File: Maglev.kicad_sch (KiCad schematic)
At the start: 33 parts, among them J1 USB_C_Receptacle, J2 691103110002, J3 61300621121, J4 61300821121, U1 WE-TVS-82400102, U2 ESP32-C3

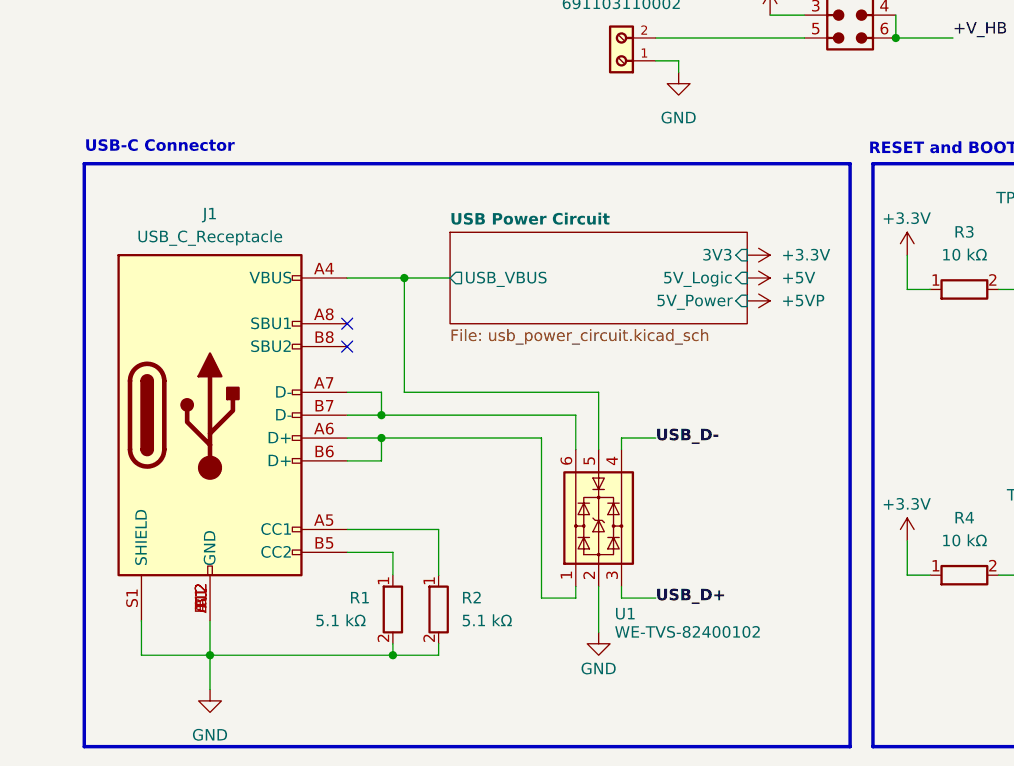
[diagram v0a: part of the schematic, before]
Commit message: cleared some rule checker errors
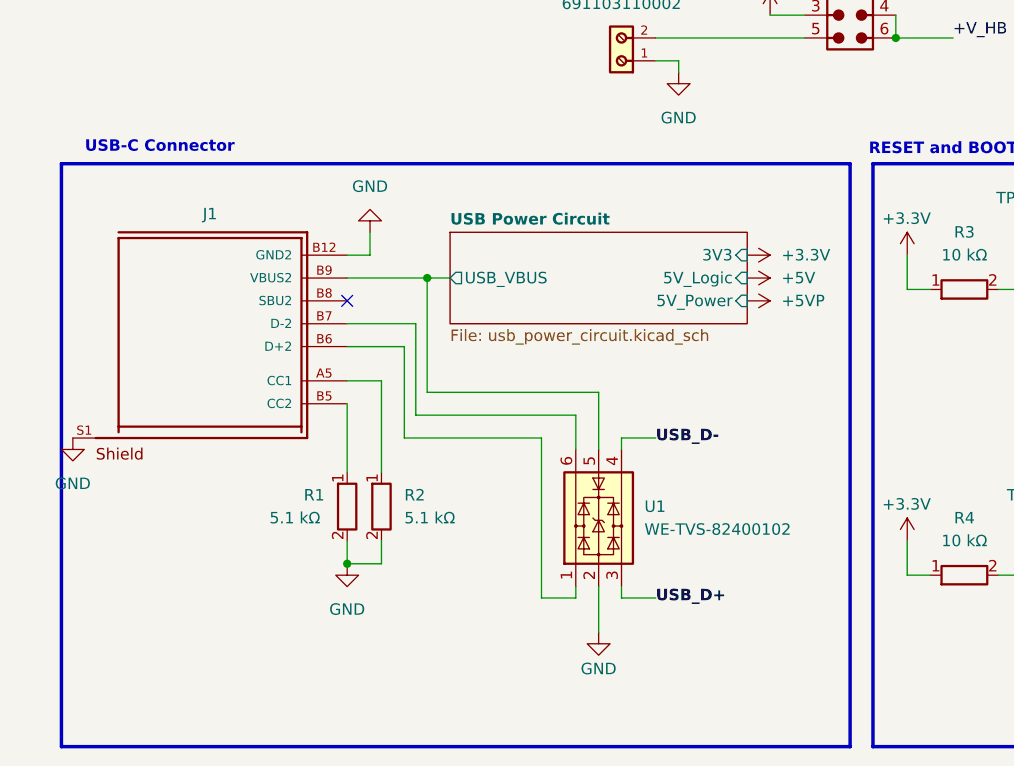
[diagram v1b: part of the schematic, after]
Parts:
- removed J1: USB_C_Receptacle, WURTH_USB:629722000214, symbol Connector:USB_C_Receptacle_USB2.0
- added J1: 629722000214, WURTH_USB:629722000214, symbol 629722000214:629722000214
- U1: footprint SOT95P280X116-6N:SOT95P280X116-6N -> Package_TO_SOT_SMD:SOT-23-6
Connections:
- net GND: now also J1.A1 (GND), J1.A12 (GND1), J1.B1 (GND3), J1.B12 (GND2), J1.S1, J1.S2, J1.S3, J1.S4
- net USB Power Circuit/USB_VBUS: now also J1.A4 (VBUS), J1.A9 (VBUS1), J1.B4 (VBUS3), J1.B9 (VBUS2)
- net at R2.1: now also J1.A5 (CC1)
- net at U1.1: now also J1.A6 (D+1), J1.B6 (D+2)
- net at U1.6: now also J1.A7 (D-1), J1.B7 (D-2)
- net at R1.1: now also J1.B5 (CC2)
- new net: J1.A8 (SBU1), J1.B8 (SBU2)
- no-connect marks 5 -> 4
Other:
- moved on the sheet: R1, R2

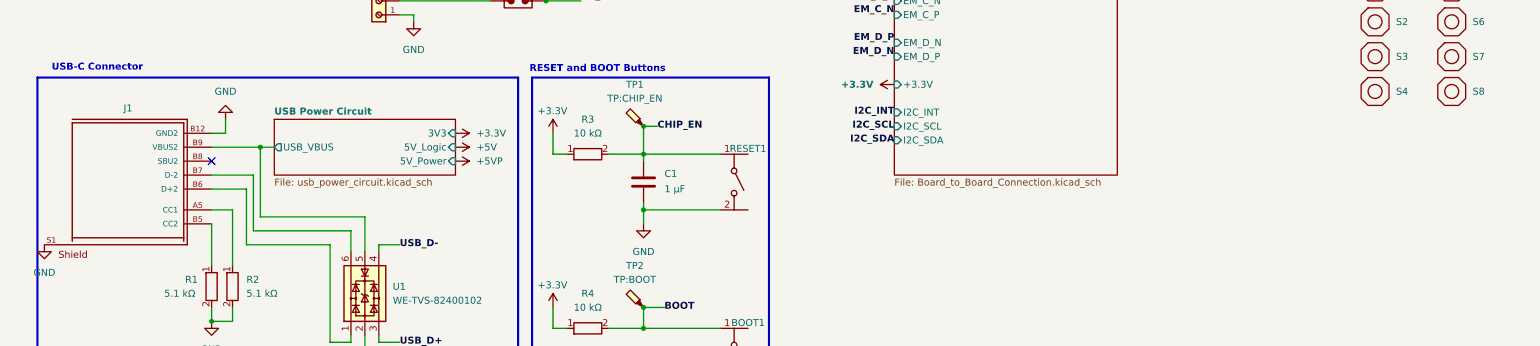
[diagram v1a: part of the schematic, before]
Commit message: Finished Testpoints, cleared all errors and warnings, changed copper thickness from 35um to 70um
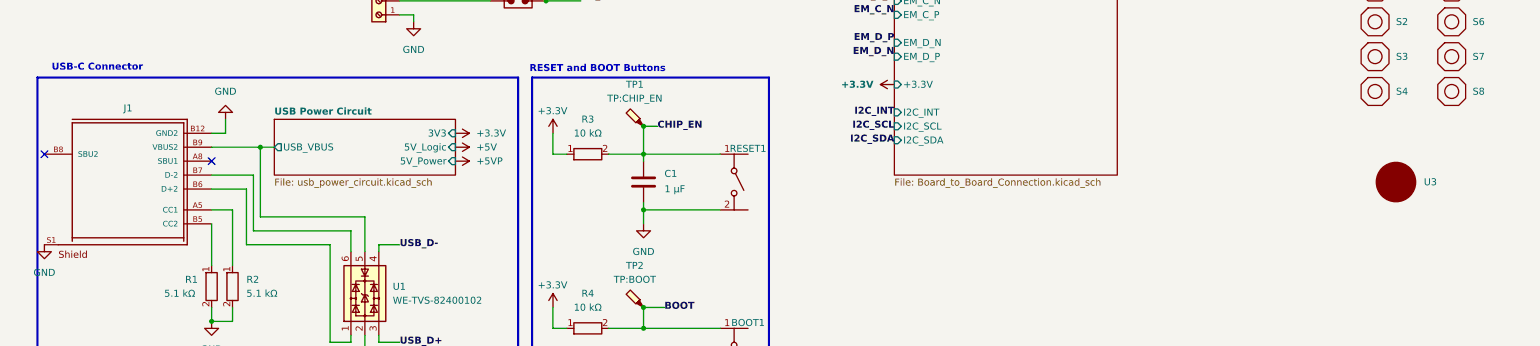
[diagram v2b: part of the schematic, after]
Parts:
- added U3: (no value), CUSTOM:MagnetRing, symbol CUSTOM:MagnetRing
- J1: footprint WURTH_USB:629722000214 -> WURTH_USB:629722000214_CUSTOM
- TP1, TP2: now left out of the parts list
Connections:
- net at J1.A8 (SBU1): no longer J1.B8 (SBU2)
- no-connect marks 4 -> 5
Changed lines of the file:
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@@
 	)
 	(no_connect
+		(at 15.24 144.78)
+	)
+	(no_connect
 		(at 64.77 24.13)
 	)
@@
 	)
 	(symbol
+		(lib_id "CUSTOM:MagnetRing")
+		(at 261.62 149.86 0)
+		(unit 1)
+		(body_style 1)
+		(exclude_from_sim no)
+		(in_bom yes)
+		(on_board yes)
+		(in_pos_files yes)
+		(dnp no)
+		(fields_autoplaced yes)
+		(property "Reference" "U3"
+			(at 266.7 149.8599 0)
+			(show_name no)
+			(do_not_autoplace no)
+			(effects
+				(font
+					(size 1.27 1.27)
+				)
+				(justify left)
+			)
+		)
+		(property "Value" ""
+			(at 261.62 149.86 0)
+			(show_name no)
+			(do_not_autoplace no)
+			(effects
+				(font
+					(size 1.27 1.27)
+				)
+			)
+		)
+		(property "Footprint" "CUSTOM:MagnetRing"
+			(at 261.62 149.86 0)
+			(hide yes)
+			(show_name no)
+			(do_not_autoplace no)
+			(effects
+				(font
+					(size 1.27 1.27)
+				)
+			)
+		)
+		(property "Datasheet" ""
+			(at 261.62 149.86 0)
+			(hide yes)
+			(show_name no)
+			(do_not_autoplace no)
+			(effects
+				(font
+					(size 1.27 1.27)
+				)
+			)
+		)
+		(property "Description" ""
+			(at 261.62 149.86 0)
+			(hide yes)
+			(show_name no)
+			(do_not_autoplace no)
+			(effects
+				(font
+					(size 1.27 1.27)
+				)
+			)
+		)
+		(instances
+			(project "Maglev"
+				(path "/cf460145-35f8-4019-907e-b966a2c32625"
+					(reference "U3")
+					(unit 1)
+				)
+			)
+		)
+	)
+	(symbol
 		(lib_id "power:GND")
 		(at 124.46 81.28 0)
@@
 		(body_style 1)
 		(exclude_from_sim no)
-		(in_bom yes)
+		(in_bom no)
 		(on_board yes)
-		(in_pos_files yes)
+		(in_pos_files no)
 		(dnp no)
 		(fields_autoplaced yes)
@@
 			)
 		)
-		(property "Footprint" "WURTH_USB:629722000214"
+		(property "Footprint" "WURTH_USB:629722000214_CUSTOM"
 			(at 30.48 148.59 0)
 			(hide yes)
@@
 		(body_style 1)
 		(exclude_from_sim no)
-		(in_bom yes)
+		(in_bom no)
 		(on_board yes)
-		(in_pos_files yes)
+		(in_pos_files no)
 		(dnp no)
 		(fields_autoplaced yes)

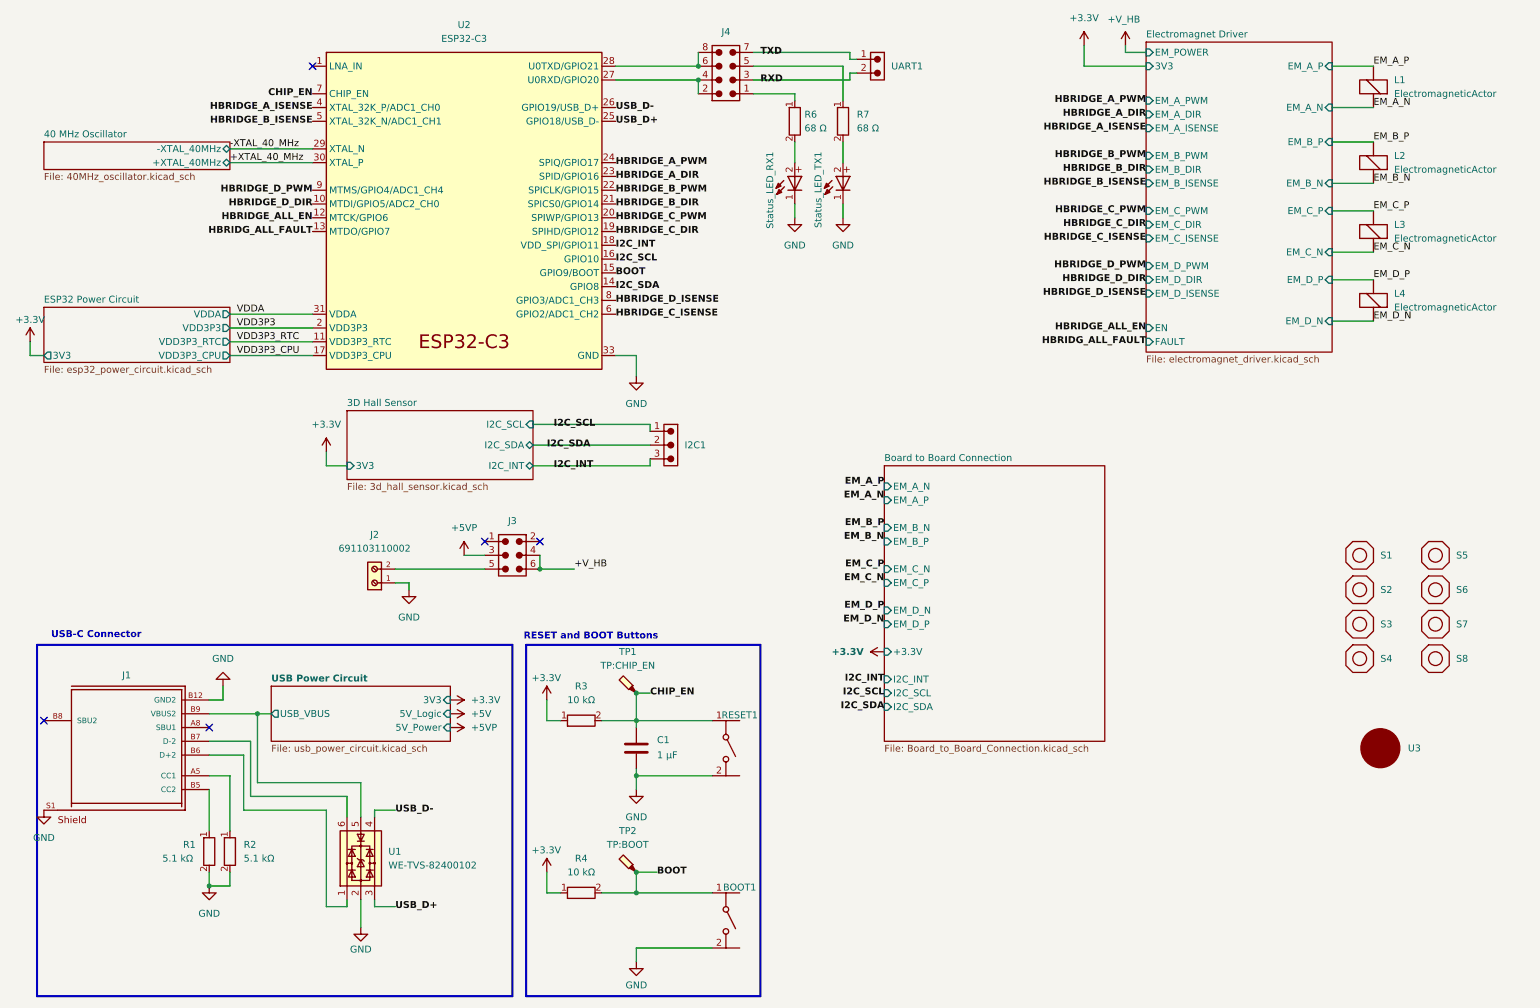
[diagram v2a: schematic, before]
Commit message: cleared some ERC errors/warnings in schematic, still one main error category to be solved
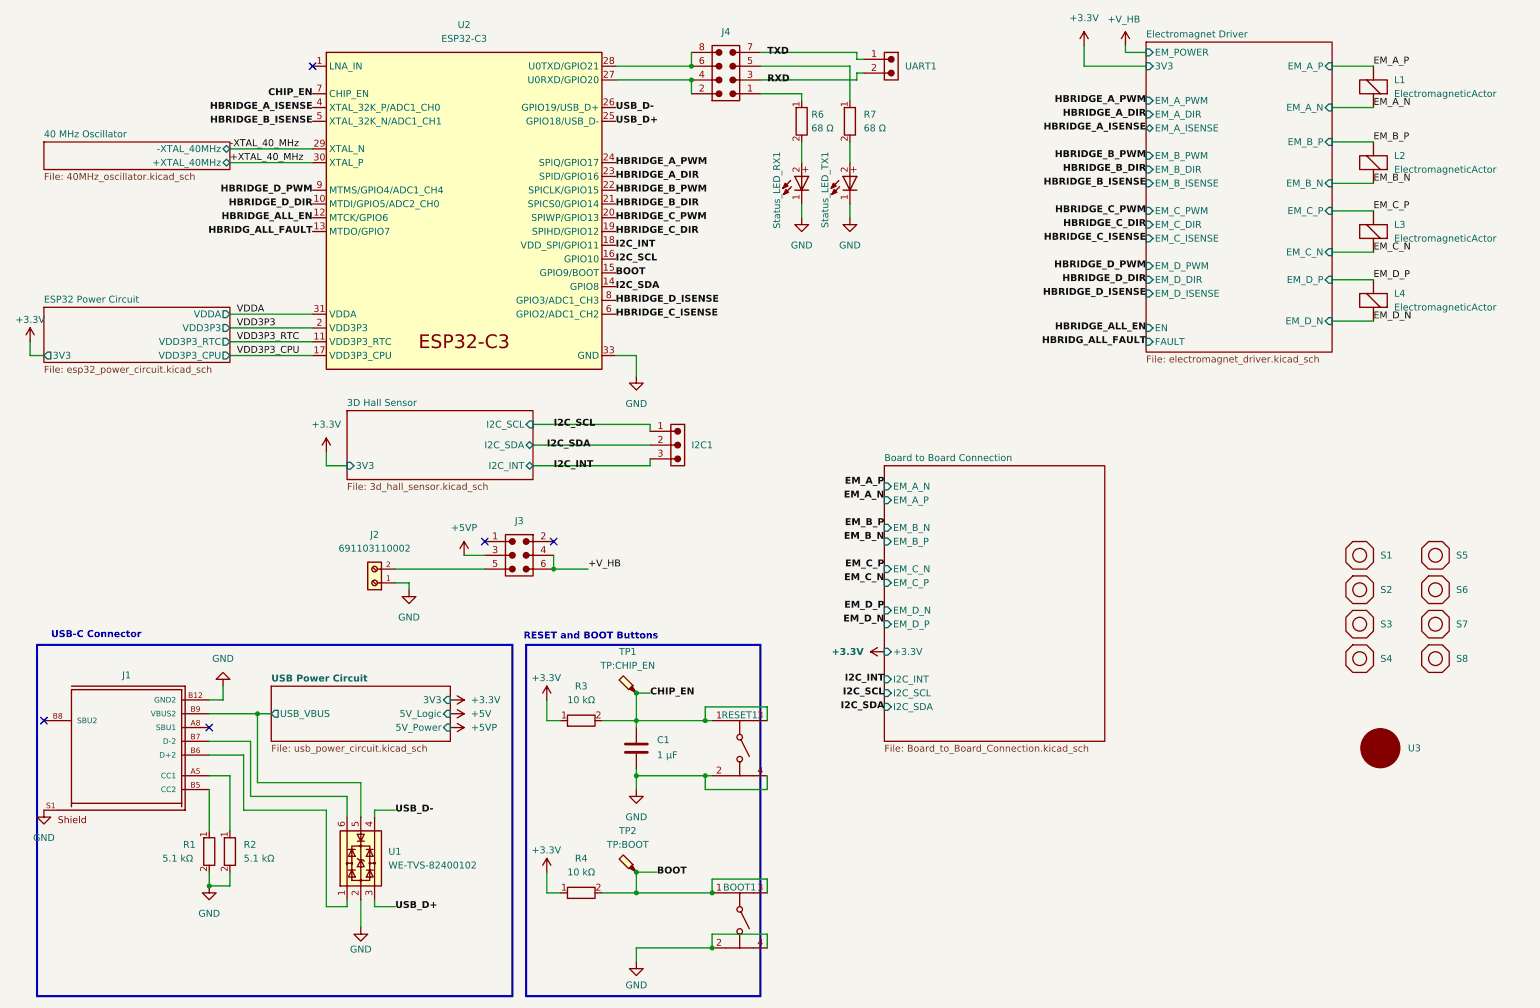
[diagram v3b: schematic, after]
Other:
- moved on the sheet: I2C1, J3, R6, R7, Status_LED_RX1, Status_LED_TX1, UART1

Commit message: wrong footprint on esp32 and misrouting on usb signals -> correctet error but routing needs to be adjusted
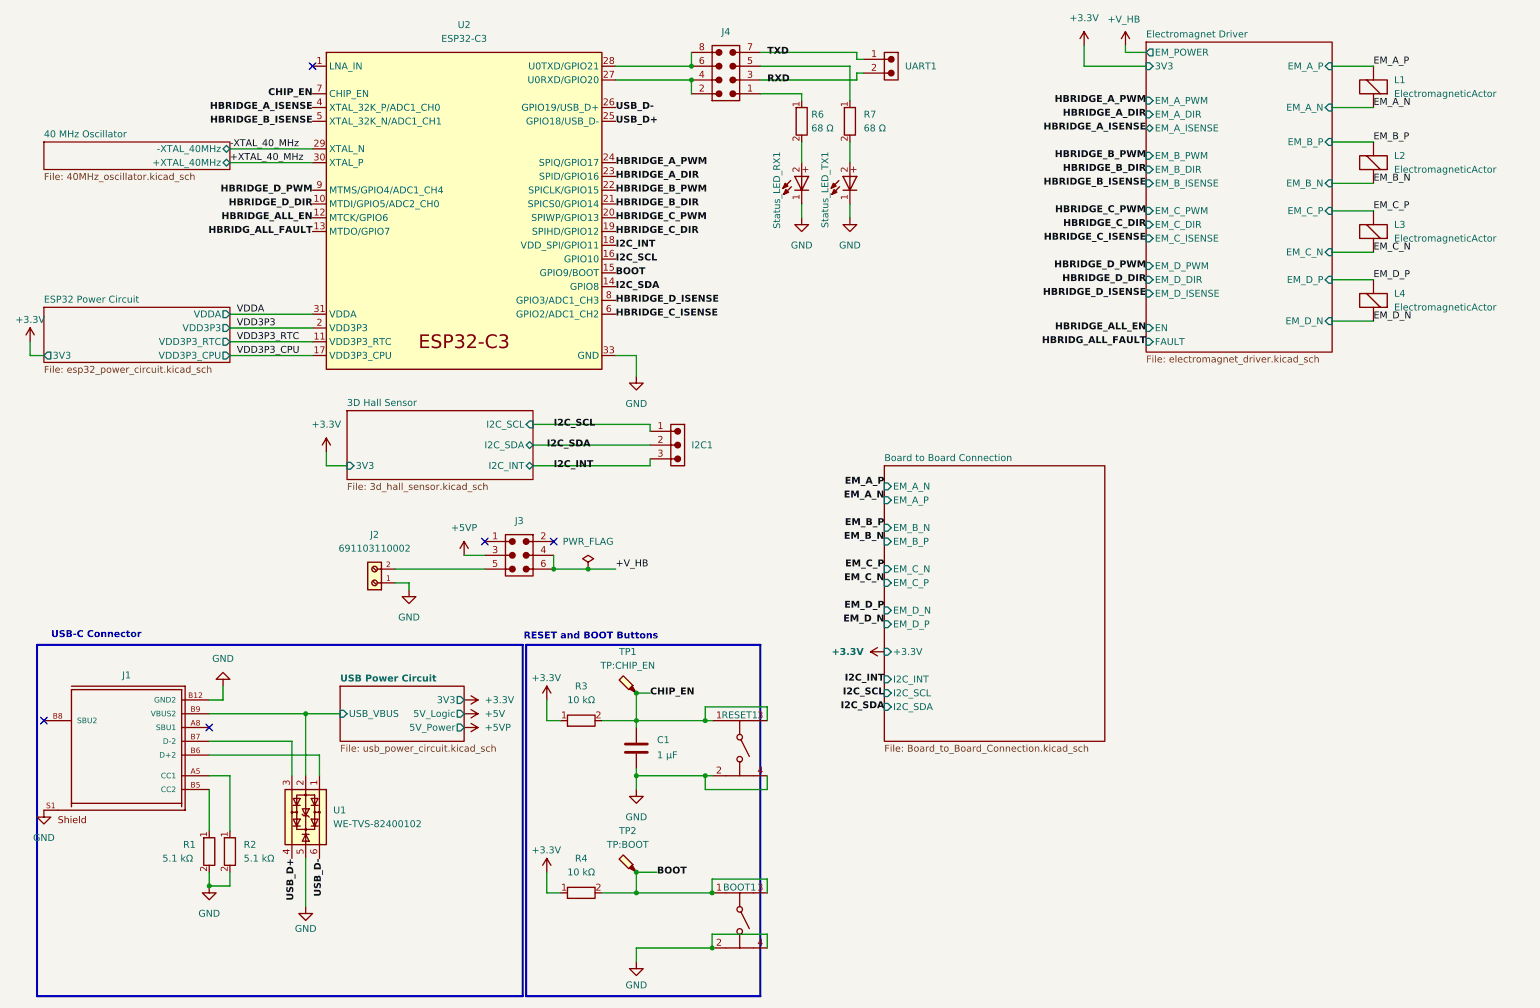
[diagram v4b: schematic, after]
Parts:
- removed S1, S2, S3, S4: (no value), CUSTOM:Spacer_15mm, symbol CUSTOM:Spacer
- removed S5, S6, S7, S8: (no value), CUSTOM:Spacer_20mm, symbol CUSTOM:Spacer
- removed U3: (no value), CUSTOM:MagnetRing, symbol CUSTOM:MagnetRing
- U2: footprint ESP32-C3FH4:QFN50P500X500X90-33N -> PCM_Espressif:QFN-32-1EP_4x4mm_P0.4mm_EP2.9x2.9mm
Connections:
- net GND: now also U1.5; no longer U1.2
- net USB Power Circuit/USB_VBUS: now also U1.2; no longer U1.5
- net USB_D+: now also U1.4; no longer U1.3
- net USB_D-: now also U1.6; no longer U1.4
- net at J1.A7 (D-1), J1.B7 (D-2): now also U1.3; no longer U1.6
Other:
- moved on the sheet: U1
